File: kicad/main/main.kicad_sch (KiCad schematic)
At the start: 52 parts, among them J1 USB_C_Receptacle_USB2.0, J10 I2C_1, J11 drib-kick, J12 drib-kick, J13 5V OUT, J14 LINE, J2 I2C_2, J3 Power IN, J4 MD1, J5 MD2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

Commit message: fix:
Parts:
- gave numbers to parts that had none: 1
- renumbered J11 to J10, J12 to J11, J13 to J12, J14 to J13, J9 to J8, J10 to J9

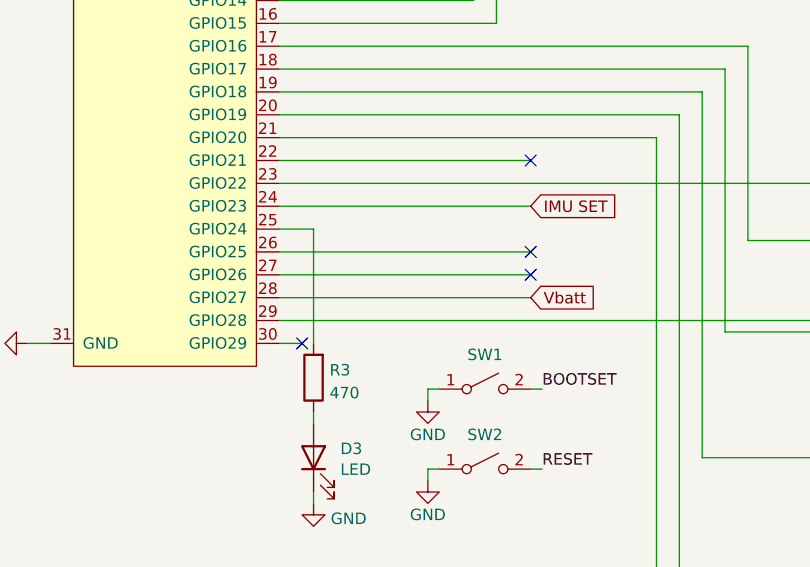
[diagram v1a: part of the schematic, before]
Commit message: LED_BUILTIN -> GPIO25
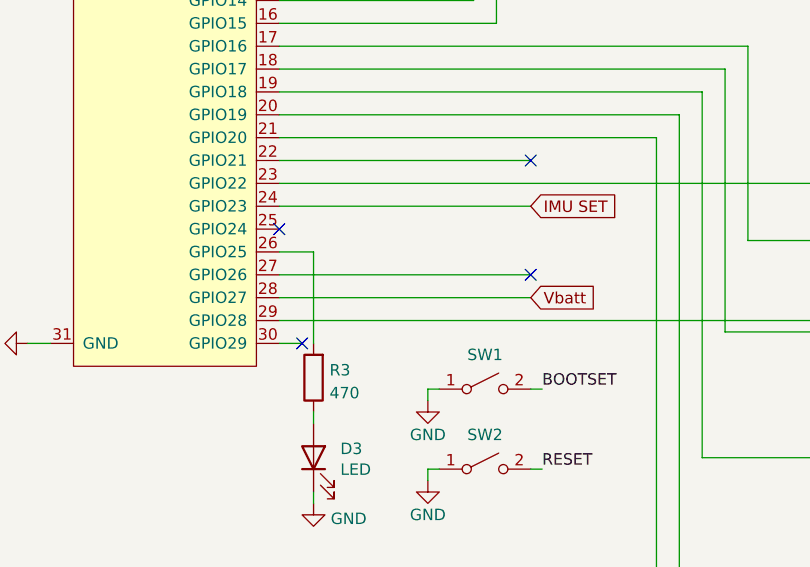
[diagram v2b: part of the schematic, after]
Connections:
- net at R3.2: now also U1.26 (GPIO25); no longer U1.25 (GPIO24)
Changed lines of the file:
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@@
   (no_connect (at 139.7 158.75))
   (no_connect (at 139.7 135.89))
+  (no_connect (at 175.26 191.77))
   (no_connect (at 139.7 161.29))
   (no_connect (at 203.2 184.15))
@@
   (no_connect (at 52.07 53.34))
   (no_connect (at 52.07 55.88))
-  (no_connect (at 203.2 194.31))
   (bus_entry (at 228.6 27.94) (size -2.54 2.54)
     (stroke (width 0) (type default) (color 0 0 0 0))
@@
     (stroke (width 0) (type default) (color 0 0 0 0))
   )
-  (wire (pts (xy 175.26 194.31) (xy 203.2 194.31))
+  (wire (pts (xy 175.26 194.31) (xy 179.07 194.31))
     (stroke (width 0) (type default) (color 0 0 0 0))
   )
@@
     (stroke (width 0) (type default) (color 0 0 0 0))
   )
+  (wire (pts (xy 179.07 194.31) (xy 179.07 204.47))
+    (stroke (width 0) (type default) (color 0 0 0 0))
+  )
   (wire (pts (xy 218.44 90.17) (xy 218.44 109.22))
     (stroke (width 0) (type default) (color 0 0 0 0))
@@
     (stroke (width 0) (type default) (color 0 0 0 0))
   )
-  (wire (pts (xy 179.07 191.77) (xy 179.07 204.47))
-    (stroke (width 0) (type default) (color 0 0 0 0))
-  )
   (wire (pts (xy 69.85 121.92) (xy 74.93 121.92))
     (stroke (width 0) (type default) (color 0 0 0 0))
@@
     (stroke (width 0) (type default) (color 0 0 0 0))
   )
-  (wire (pts (xy 175.26 191.77) (xy 179.07 191.77))
-    (stroke (width 0) (type default) (color 0 0 0 0))
-  )

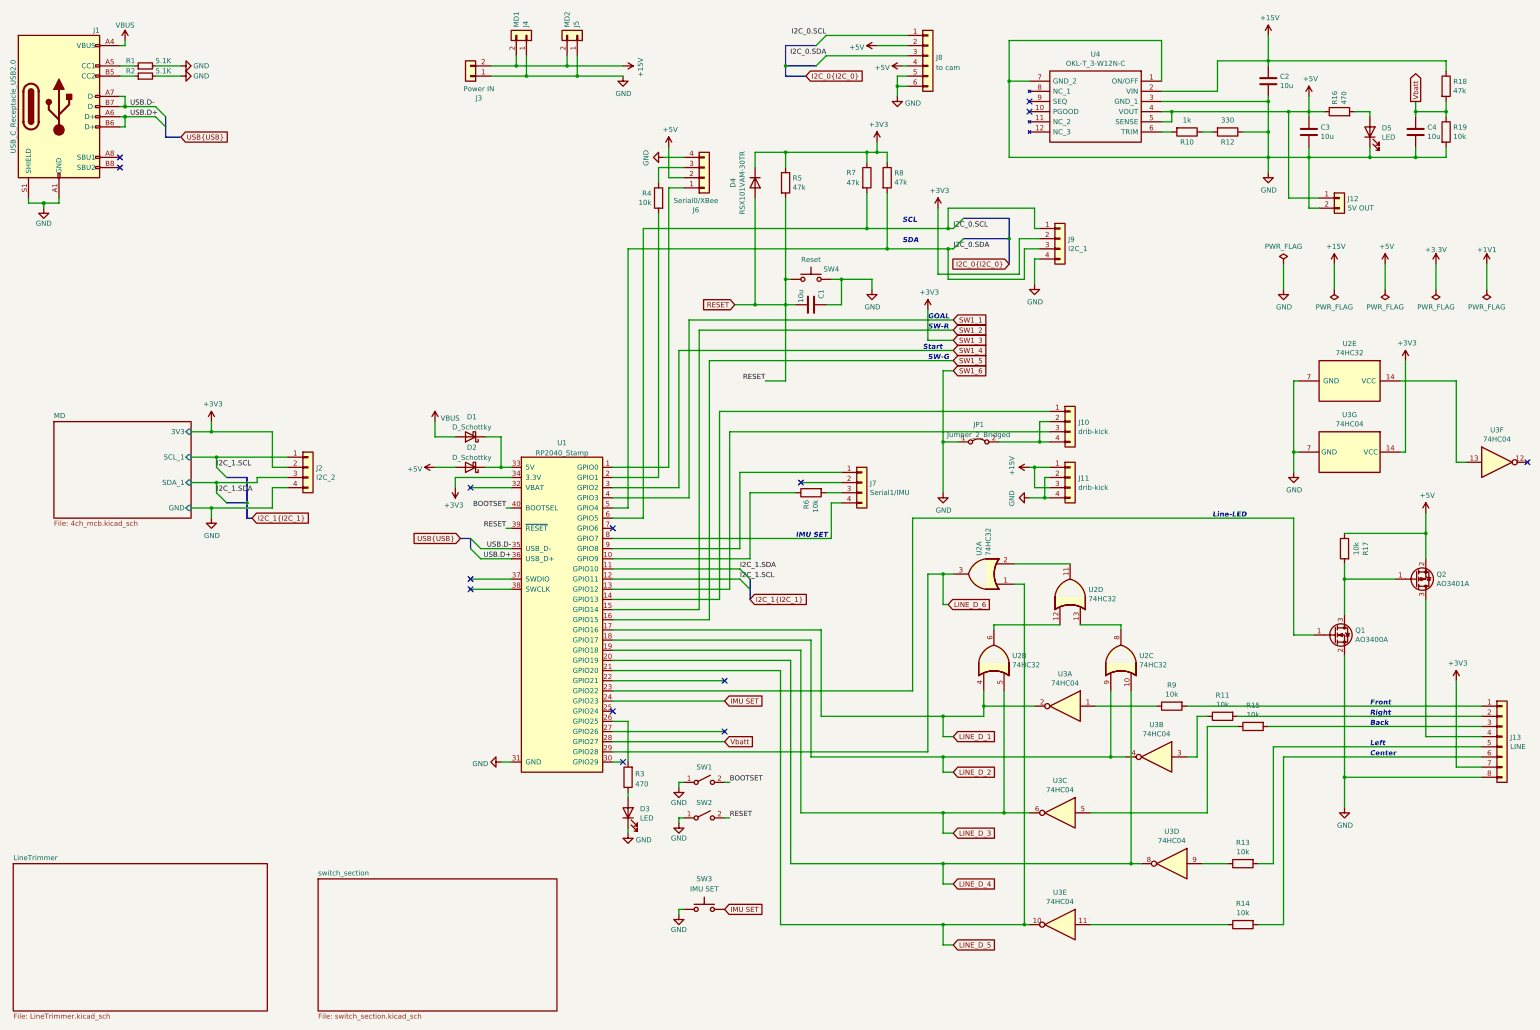
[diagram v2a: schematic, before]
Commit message: fix: vison-board GND
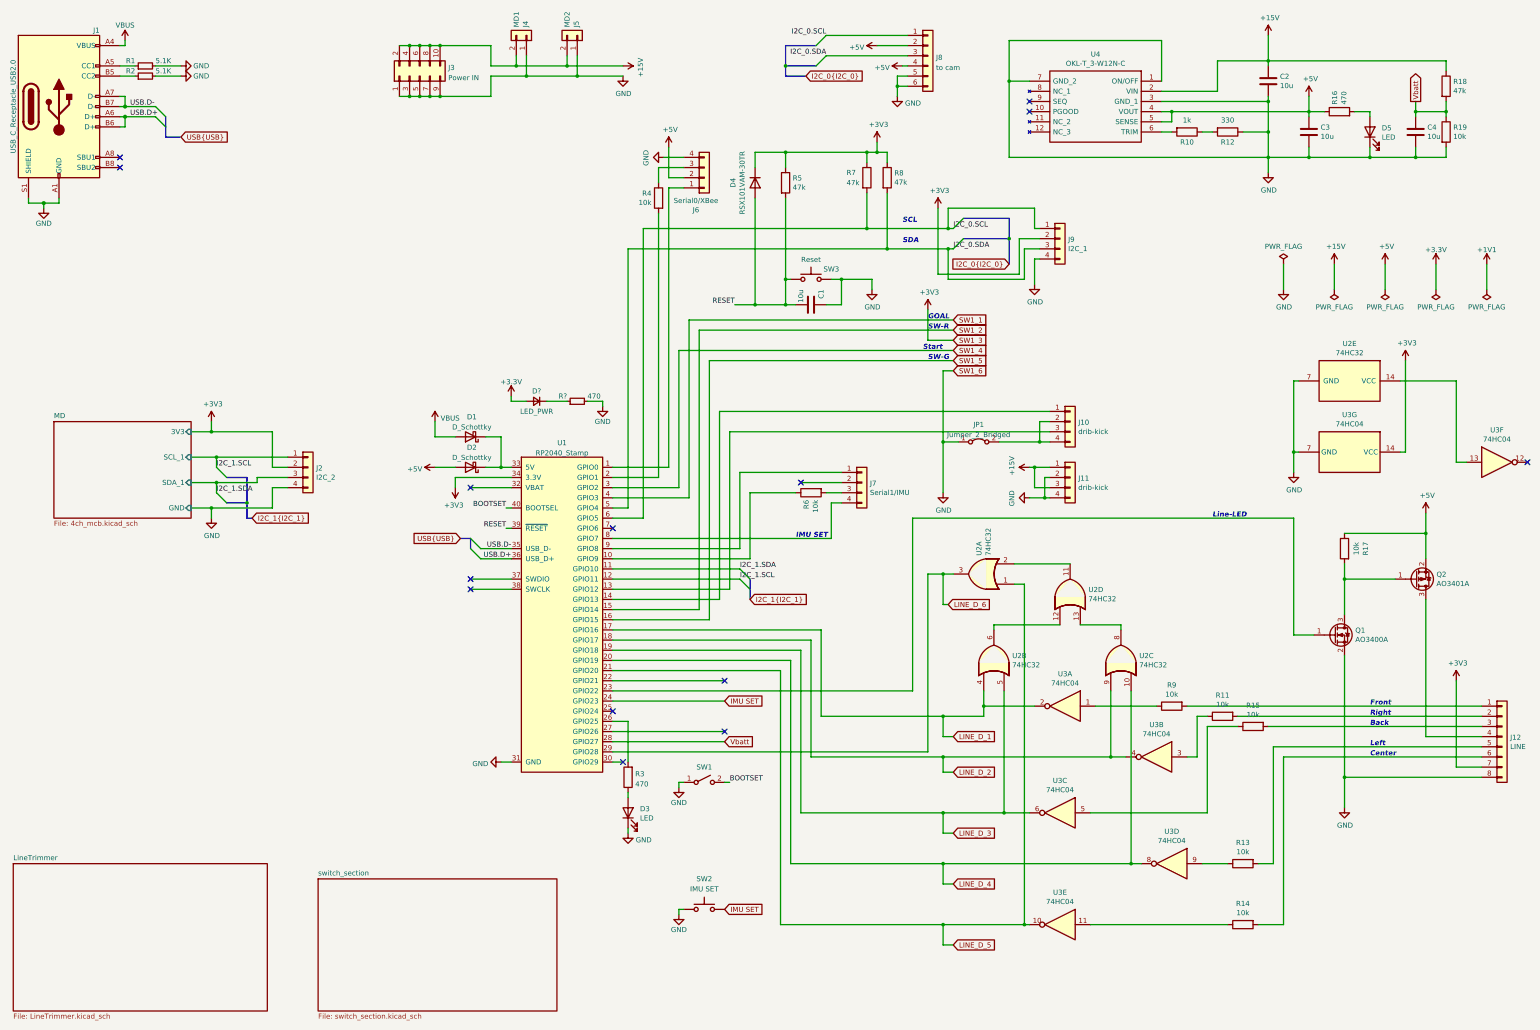
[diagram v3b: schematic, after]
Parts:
- removed J12: 5V OUT, Connector_JST:JST_XH_B2B-XH-A_1x02_P2.50mm_Vertical, symbol Connector_Generic:Conn_01x02
- removed J3: Power IN, Connector_JST:JST_VH_B2P-VH-B_1x02_P3.96mm_Vertical, symbol Connector_Generic:Conn_01x02
- removed SW2: BTN_UP, Button_Switch_SMD:Panasonic_EVQPUJ_EVQPUA, symbol Switch:SW_SPST
- added D?: LED_PWR, 0.main.robot:LED_SMLE13WBC8W1, symbol Device:D_Small
- added J3: Power IN, Connector_PinSocket_2.54mm:PinSocket_2x05_P2.54mm_Vertical, symbol Connector_Generic:Conn_02x05_Odd_Even
- added R?: 470, Resistor_SMD:R_0603_1608Metric_Pad0.98x0.95mm_HandSolder, symbol Device:R_Small
- JP1: footprint (none) -> Connector_PinHeader_1.27mm:PinHeader_1x02_P1.27mm_Vertical
- SW1: value BTN_UP -> BOOTSET
- U1: footprint (none) -> rp2040_stamp:RP2040_Stamp_SMD
- renumbered J13 to J12, SW3 to SW2, SW4 to SW3
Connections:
- net +15V: now also J3.10 (Pin_10), J3.2 (Pin_2), J3.4 (Pin_4), J3.6 (Pin_6), J3.8 (Pin_8)
- net +3.3V: now also D?.2 (A)
- net GND: now also J3.1 (Pin_1), J3.3 (Pin_3), J3.5 (Pin_5), J3.7 (Pin_7), J3.9 (Pin_9), R?.2
- new net: D?.1 (K), R?.1

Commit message: fix: main
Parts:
- J7: footprint 0.main.robot:JSTB4B-ZR -> Connector_PinHeader_2.54mm:PinHeader_1x04_P2.54mm_Vertical
- SW1: footprint Button_Switch_SMD:Panasonic_EVQPUJ_EVQPUA -> 0.main.robot:THAU13-AB-R
- gave numbers to parts that had none: 2
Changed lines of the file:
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@@
   (symbol (lib_id "Device:R_Small") (at 166.37 114.3 90) (unit 1)
     (in_bom yes) (on_board yes)
-    (property "Reference" "R?" (id 0) (at 163.83 113.03 90)
+    (property "Reference" "R43" (id 0) (at 163.83 113.03 90)
       (effects (font (size 1.27 1.27)) (justify left))
     )
@@
   (symbol (lib_id "power:GND") (at 172.72 115.57 0) (unit 1)
     (in_bom yes) (on_board yes)
-    (property "Reference" "#PWR?" (id 0) (at 172.72 121.92 0)
+    (property "Reference" "#PWR065" (id 0) (at 172.72 121.92 0)
       (effects (font (size 1.27 1.27)) hide)
     )
@@
       (effects (font (size 1.27 1.27)) (justify left))
     )
-    (property "Footprint" "0.main.robot:JSTB4B-ZR" (id 2) (at 237.49 134.62 0)
+    (property "Footprint" "Connector_PinHeader_2.54mm:PinHeader_1x04_P2.54mm_Vertical" (id 2) (at 237.49 134.62 0)
       (effects (font (size 1.27 1.27)) hide)
     )
@@
   (symbol (lib_id "Device:D_Small") (at 156.21 114.3 0) (mirror y) (unit 1)
     (in_bom yes) (on_board yes)
-    (property "Reference" "D?" (id 0) (at 156.21 111.76 0))
+    (property "Reference" "D18" (id 0) (at 156.21 111.76 0))
     (property "Value" "LED_PWR" (id 1) (at 156.21 116.84 0))
     (property "Footprint" "0.main.robot:LED_SMLE13WBC8W1" (id 2) (at 156.21 114.3 90)
@@
       (effects (font (size 1.27 1.27)) hide)
     )
-    (property "Footprint" "Button_Switch_SMD:Panasonic_EVQPUJ_EVQPUA" (id 2) (at 198.12 209.55 0)
+    (property "Footprint" "0.main.robot:THAU13-AB-R" (id 2) (at 198.12 209.55 0)
       (effects (font (size 1.27 1.27)) hide)
     )
@@
   (symbol (lib_id "power:+3.3V") (at 149.86 113.03 0) (unit 1)
     (in_bom yes) (on_board yes) (fields_autoplaced)
-    (property "Reference" "#PWR?" (id 0) (at 149.86 116.84 0)
+    (property "Reference" "#PWR064" (id 0) (at 149.86 116.84 0)
       (effects (font (size 1.27 1.27)) hide)
     )
@@
       (reference "#PWR063") (unit 1) (value "GND") (footprint "")
     )
+    (path "/d888b6b5-2e13-4f4b-ab01-6ff9b57471ea"
+      (reference "#PWR064") (unit 1) (value "+3.3V") (footprint "")
+    )
     (path "/1fa32b86-23a9-4821-8971-828d501e3aba"
-      (reference "#PWR?") (unit 1) (value "GND") (footprint "")
-    )
-    (path "/d888b6b5-2e13-4f4b-ab01-6ff9b57471ea"
-      (reference "#PWR?") (unit 1) (value "+3.3V") (footprint "")
+      (reference "#PWR065") (unit 1) (value "GND") (footprint "")
     )
     (path "/16d45733-181d-4e84-890c-996ba99a2a5b"
@@
     )
     (path "/8ec63555-7cdc-4bf3-ae27-56e92cc8a99f"
-      (reference "D?") (unit 1) (value "LED_PWR") (footprint "0.main.robot:LED_SMLE13WBC8W1")
+      (reference "D18") (unit 1) (value "LED_PWR") (footprint "0.main.robot:LED_SMLE13WBC8W1")
     )
     (path "/262a0d4b-3c87-49ab-815d-dea6b7ca370a"
@@
     )
     (path "/64918e7a-0abb-4f6f-9852-97bcf130e83b"
-      (reference "J7") (unit 1) (value "Serial1/IMU") (footprint "0.main.robot:JSTB4B-ZR")
+      (reference "J7") (unit 1) (value "Serial1/IMU") (footprint "Connector_PinHeader_2.54mm:PinHeader_1x04_P2.54mm_Vertical")
     )
     (path "/05c35a87-473b-4928-9233-cb895723bf3b"
@@
     )
     (path "/0cabb643-a707-4797-a2c9-800dfbd5b6e0"
-      (reference "R?") (unit 1) (value "470") (footprint "Resistor_SMD:R_0603_1608Metric_Pad0.98x0.95mm_HandSolder")
+      (reference "R43") (unit 1) (value "470") (footprint "Resistor_SMD:R_0603_1608Metric_Pad0.98x0.95mm_HandSolder")
     )
     (path "/54dc5971-37b9-46a7-8049-349fe99f9b14/e15ab46d-42eb-474f-881c-556db992e495"
@@
     )
     (path "/b2e282c1-a5e8-4e36-99f2-47e1029dac07"
-      (reference "SW1") (unit 1) (value "BOOTSET") (footprint "Button_Switch_SMD:Panasonic_EVQPUJ_EVQPUA")
+      (reference "SW1") (unit 1) (value "BOOTSET") (footprint "0.main.robot:THAU13-AB-R")
     )
     (path "/0e1c0f6f-9b3d-4dd0-b1e3-45fdfc5a7186"
@@
     )
     (path "/54dc5971-37b9-46a7-8049-349fe99f9b14/309bea1d-c82d-47c5-8e89-2f171f0dac3f"
-      (reference "SW4") (unit 1) (value "RESET") (footprint "0.main.robot:TVAF06-A020B-R")
+      (reference "SW4") (unit 1) (value "RESET") (footprint "0.main.robot:THAU13-AB-R")
     )
     (path "/70fde810-700d-485a-8c97-2da167292bf1/00000000-0000-0000-0000-00005f3ebb0e"

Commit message: PCB 修正
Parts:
- added J21: GND-Test, Connector_PinHeader_2.54mm:PinHeader_1x01_P2.54mm_Vertical, symbol Connector_Generic:Conn_01x01
- D3: value LED -> LED_BUILTIN
- D4: footprint Diode_SMD:D_SMA -> Diode_SMD:D_0805_2012Metric_Pad1.15x1.40mm_HandSolder
- D5: value LED -> 5V
- JP1: footprint Connector_PinHeader_1.27mm:PinHeader_1x02_P1.27mm_Vertical -> Jumper:SolderJumper-2_P1.3mm_Bridged2Bar_RoundedPad1.0x1.5mm
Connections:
- net GND: now also J21.1 (Pin_1)
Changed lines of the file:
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@@
   (title_block
     (title "main board")
-    (date "2022-12-10")
+    (date "2023-03-03")
     (rev "V1.0")
     (company "A.Saeki")
@@
     (property "Reference" "D4" (id 0) (at 205.3082 59.69 0))
     (property "Value" "RSX101VAM-30TR" (id 1) (at 207.6196 59.69 0))
-    (property "Footprint" "Diode_SMD:D_SMA" (id 2) (at 206.375 59.69 0)
+    (property "Footprint" "Diode_SMD:D_0805_2012Metric_Pad1.15x1.40mm_HandSolder" (id 2) (at 206.375 59.69 0)
       (effects (font (size 1.27 1.27)) hide)
     )
@@
       (effects (font (size 1.27 1.27)) (justify right))
     )
-    (property "Value" "LED" (id 1) (at 367.4618 48.3108 90)
+    (property "Value" "5V" (id 1) (at 367.4618 48.3108 90)
       (effects (font (size 1.27 1.27)) (justify right))
     )
@@
     (property "Reference" "JP1" (id 0) (at 266.7 120.1252 0))
     (property "Value" "Jumper_2_Bridged" (id 1) (at 266.7 122.6621 0))
-    (property "Footprint" "Connector_PinHeader_1.27mm:PinHeader_1x02_P1.27mm_Vertical" (id 2) (at 266.7 124.46 0)
+    (property "Footprint" "Jumper:SolderJumper-2_P1.3mm_Bridged2Bar_RoundedPad1.0x1.5mm" (id 2) (at 266.7 124.46 0)
       (effects (font (size 1.27 1.27)) hide)
     )
@@
     (pin "2")
   )
+  (symbol (lib_id "Connector_Generic:Conn_01x01") (at 166.37 38.1 270) (unit 1)
+    (in_bom yes) (on_board yes) (fields_autoplaced)
+    (property "Reference" "J21" (id 0) (at 168.402 37.2653 90)
+      (effects (font (size 1.27 1.27)) (justify left))
+    )
+    (property "Value" "GND-Test" (id 1) (at 168.402 39.8022 90)
+      (effects (font (size 1.27 1.27)) (justify left))
+    )
+    (property "Footprint" "Connector_PinHeader_2.54mm:PinHeader_1x01_P2.54mm_Vertical" (id 2) (at 166.37 38.1 0)
+      (effects (font (size 1.27 1.27)) hide)
+    )
+    (property "Datasheet" "~" (id 3) (at 166.37 38.1 0)
+      (effects (font (size 1.27 1.27)) hide)
+    )
+    (pin "1")
+  )
   (symbol (lib_id "Connector_Generic:Conn_01x02") (at 153.67 22.86 270) (mirror x) (unit 1)
     (in_bom yes) (on_board yes)
@@
       (effects (font (size 1.27 1.27)) (justify right))
     )
-    (property "Value" "LED" (id 1) (at 182.0418 218.4908 90)
+    (property "Value" "LED_BUILTIN" (id 1) (at 182.0418 218.4908 90)
       (effects (font (size 1.27 1.27)) (justify right))
     )
@@
     )
     (path "/ce04b34d-5ca8-41d1-b396-b8c198818c77"
-      (reference "D3") (unit 1) (value "LED") (footprint "0.main.robot:LED_SMLE13WBC8W1")
+      (reference "D3") (unit 1) (value "LED_BUILTIN") (footprint "0.main.robot:LED_SMLE13WBC8W1")
     )
     (path "/41caf97f-c01d-49b8-8225-611c11850817"
-      (reference "D4") (unit 1) (value "RSX101VAM-30TR") (footprint "Diode_SMD:D_SMA")
+      (reference "D4") (unit 1) (value "RSX101VAM-30TR") (footprint "Diode_SMD:D_0805_2012Metric_Pad1.15x1.40mm_HandSolder")
     )
     (path "/6601d461-d011-4d4b-a61a-f1085c7c1e41"
-      (reference "D5") (unit 1) (value "LED") (footprint "0.main.robot:LED_SMLE13WBC8W1")
+      (reference "D5") (unit 1) (value "5V") (footprint "0.main.robot:LED_SMLE13WBC8W1")
     )
     (path "/17adc8c0-c792-4780-aab1-71d31733c779/1d2499f9-a2d0-4379-9614-5fd25bc3fe1f"
@@
       (reference "J20") (unit 1) (value "Trimmer") (footprint "0.main.robot:JSTB6B-ZR")
     )
+    (path "/989cf0ea-bbae-4e3e-bdeb-b13cacdeeaa9"
+      (reference "J21") (unit 1) (value "GND-Test") (footprint "Connector_PinHeader_2.54mm:PinHeader_1x01_P2.54mm_Vertical")
+    )
     (path "/8f35d220-c53a-42e9-9bdd-e2fe7cb741d3"
-      (reference "JP1") (unit 1) (value "Jumper_2_Bridged") (footprint "Connector_PinHeader_1.27mm:PinHeader_1x02_P1.27mm_Vertical")
+      (reference "JP1") (unit 1) (value "Jumper_2_Bridged") (footprint "Jumper:SolderJumper-2_P1.3mm_Bridged2Bar_RoundedPad1.0x1.5mm")
     )
     (path "/70fde810-700d-485a-8c97-2da167292bf1/00000000-0000-0000-0000-000061873e0d"
